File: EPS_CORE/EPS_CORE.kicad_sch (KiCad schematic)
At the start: 29 parts, among them J6301 VBUS, J7101 VBUS, J7102 BATT_PACK, J7103 BATT_PACK, J7104 VBUS, J7105 Chan, J7106 Chan, SW7101 Deploy, U7101 LP38690SDX-3.3/NOPB

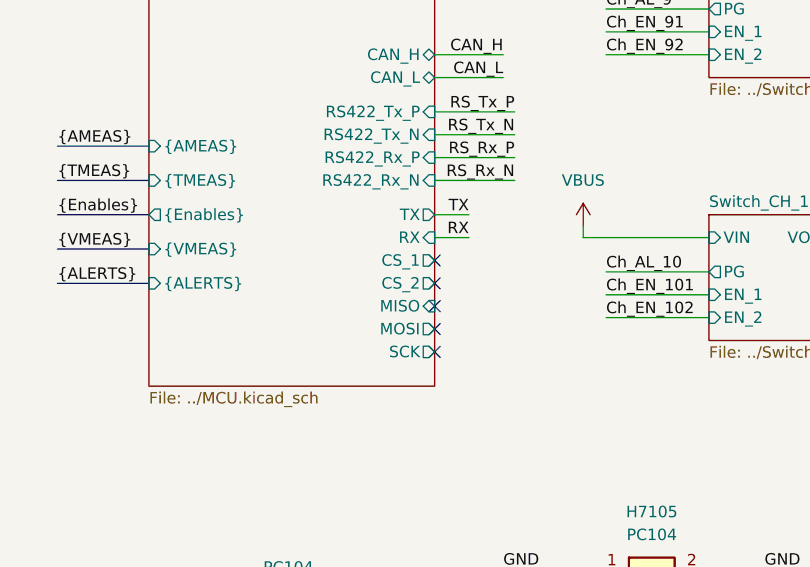
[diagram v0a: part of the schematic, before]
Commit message: added universal switch, added simples current source, reworked test schematic and pcb
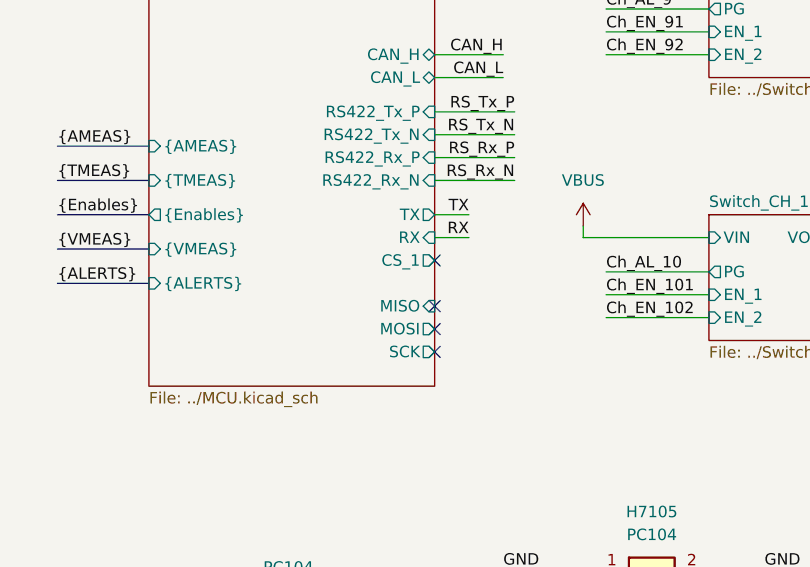
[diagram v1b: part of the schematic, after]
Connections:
- no-connect marks 23 -> 22
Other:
- sheet MCU ports: added none; removed CS_2
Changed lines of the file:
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@@
 	)
 	(no_connect
-		(at 184.15 60.96)
-	)
-	(no_connect
 		(at 250.19 118.11)
 	)
@@
 			(effects
 				(font
-					(size 1.27 1.27)
-				)
-				(justify right)
-			)
-		)
-		(pin "CS_2" output
-			(at 184.15 60.96 0)
-			(effects
-				(font

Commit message: progress on CORE pcb
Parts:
- removed J6301, J7104: VBUS, Connector_Harwin:Harwin_Gecko-G125-FVX1205L0X_2x06_P1.25mm_Vertical, symbol Connector_Generic:Conn_02x06_Top_Bottom
- removed J7105, J7106: Chan, Connector_Molex:Molex_CLIK-Mate_502494-0470_1x04-1MP_P2.00mm_Horizontal, symbol Connector_Generic:Conn_01x04
- added J106: OUT, Connector_Harwin:Harwin_Gecko-G125-MVX1005L1X_2x05_P1.25mm_Vertical, symbol Connector_Generic:Conn_02x05_Top_Bottom
- J105: renamed from J7101; now not fitted; now left out of the parts list
- renumbered C7106 to C101, C7101 to C102, C7105 to C103, C7103 to C104, C7102 to C105, C7104 to C106, FID7101 to FID101, FID7102 to FID102, H7105 to H101, H7106 to H102, H7101 to H103, H7102 to H104, H7103 to H105, H7104 to H106, J7102 to J102, J7103 to J104, PCB7101 to PCB101, R7104 to R101, R7105 to R102, R7101 to R103, R7102 to R104, R7103 to R105, SW7101 to SW101, U7101 to U101
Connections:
- net AMEAS_2: now also H101.5 (Pin_5); no longer H101.7 (Pin_7)
- net AMEAS_3: now also H101.7 (Pin_7); no longer H101.11 (Pin_11)
- net AMEAS_4: now also H101.9 (Pin_9); no longer H101.5 (Pin_5)
- net AMEAS_5: now also H101.11 (Pin_11); no longer H101.9 (Pin_9)
- net BUS: now also H102.41 (Pin_41), H102.42 (Pin_42), H102.43 (Pin_43), H102.44 (Pin_44), H102.45 (Pin_45), H102.46 (Pin_46)
- net Ch_EN_31: now also H102.29 (Pin_29); no longer H101.39 (Pin_39)
- net Ch_EN_32: now also H102.33 (Pin_33); no longer H101.43 (Pin_43)
- net Ch_EN_61: now also H102.31 (Pin_31); no longer H101.41 (Pin_41)
- net Ch_EN_62: now also H102.35 (Pin_35); no longer H101.45 (Pin_45)
- net Ch_EN_7x: now also H102.37 (Pin_37); no longer H101.47 (Pin_47)
- net Ch_EN_8x: now also H102.38 (Pin_38); no longer H101.49 (Pin_49)
- net Ch_V_1: now also H102.13 (Pin_13); no longer H101.22 (Pin_22)
- net Ch_V_2: now also H102.11 (Pin_11); no longer H101.26 (Pin_26)
- net Ch_V_3: now also H102.9 (Pin_9); no longer H101.30 (Pin_30)
- net Ch_V_4: now also H102.7 (Pin_7); no longer H101.24 (Pin_24)
- net Ch_V_5: now also H102.5 (Pin_5); no longer H101.28 (Pin_28)
- net Ch_V_6: now also H102.3 (Pin_3); no longer H101.32 (Pin_32)
- net Ch_V_7: now also H101.24 (Pin_24); no longer H101.34 (Pin_34)
- net Ch_V_8: now also H101.22 (Pin_22); no longer H101.36 (Pin_36)
- net Channel_10: now also J106.4 (Pin_4), J106.5 (Pin_5)
- net Channel_9: now also J106.1 (Pin_1), J106.2 (Pin_2)
- net GND: now also H101.39 (Pin_39), H101.41 (Pin_41), H101.43 (Pin_43), H101.44 (Pin_44), H101.45 (Pin_45), H101.46 (Pin_46), H101.47 (Pin_47), H101.48 (Pin_48), H101.49 (Pin_49), H101.50 (Pin_50), H102.17 (Pin_17), H102.19 (Pin_19), H102.21 (Pin_21), H102.23 (Pin_23), H102.25 (Pin_25), H102.36 (Pin_36), H102.39 (Pin_39), H102.40 (Pin_40), J106.10 (Pin_10), J106.3 (Pin_3), J106.6 (Pin_6), J106.7 (Pin_7), J106.8 (Pin_8), J106.9 (Pin_9); no longer H102.29 (Pin_29), H102.44 (Pin_44), H102.46 (Pin_46), H102.48 (Pin_48), H102.50 (Pin_50), H102.52 (Pin_52)
- net MPPT_~{EN}: now also H102.27 (Pin_27); no longer H102.17 (Pin_17)
- net SOL_EN_1: now also H101.36 (Pin_36); no longer H102.3 (Pin_3)
- net SOL_EN_2: now also H101.34 (Pin_34); no longer H102.5 (Pin_5)
- net SOL_EN_3: now also H101.32 (Pin_32); no longer H102.7 (Pin_7)
- net SOL_EN_4: now also H101.30 (Pin_30); no longer H102.9 (Pin_9)
- net SOL_EN_5: now also H101.28 (Pin_28); no longer H102.11 (Pin_11)
- net SOL_EN_6: now also H101.26 (Pin_26); no longer H102.13 (Pin_13)
- net VBUS: now also H102.48 (Pin_48), H102.50 (Pin_50), H102.52 (Pin_52); no longer H101.44 (Pin_44), H101.46 (Pin_46), H101.48 (Pin_48), H101.50 (Pin_50), H102.43 (Pin_43), H102.45 (Pin_45)
- no-connect marks 22 -> 7
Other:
- moved on the sheet: H101, H102

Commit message: nearly finnished CORE pcb
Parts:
- added FID103, FID104: Fiducial, Fiducial:Fiducial_1mm_Mask2mm, symbol Mechanical:Fiducial
- added J101: CAN, Connector_Molex:Molex_PicoBlade_53261-0471_1x04-1MP_P1.25mm_Horizontal, symbol Connector_Generic_MountingPin:Conn_01x04_MountingPin
- added J103: RS-485, Connector_Molex:Molex_PicoBlade_53261-0471_1x04-1MP_P1.25mm_Horizontal, symbol Connector_Generic_MountingPin:Conn_01x04_MountingPin
- J102, J104: footprint Connector_Harwin:Harwin_Gecko-G125-FVX1605L0X_2x08_P1.25mm_Vertical -> Outlines:G125-MH11605L1P
- J106: footprint Connector_Harwin:Harwin_Gecko-G125-MVX1005L1X_2x05_P1.25mm_Vertical -> Outlines:G125-MH11605L1P
- R101, R102: footprint Resistor_SMD:R_0603_1608Metric_Pad0.98x0.95mm_HandSolder -> Resistor_SMD:R_1210_3225Metric_Pad1.30x2.65mm_HandSolder
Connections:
- net +3V3: no longer J102.8 (Pin_8), J104.8 (Pin_8)
- net AMEAS_2: now also H102.4 (Pin_4); no longer H101.5 (Pin_5)
- net AMEAS_3: now also H101.5 (Pin_5); no longer H101.7 (Pin_7)
- net AMEAS_4: now also H102.6 (Pin_6); no longer H101.9 (Pin_9)
- net AMEAS_5: now also H101.7 (Pin_7); no longer H101.11 (Pin_11)
- net AMEAS_6: now also H102.8 (Pin_8); no longer H101.13 (Pin_13)
- net AMEAS_7: now also H101.9 (Pin_9); no longer H101.15 (Pin_15)
- net AMEAS_8: now also H102.10 (Pin_10); no longer H101.17 (Pin_17)
- net AMEAS_SOL_1: now also H101.17 (Pin_17); no longer H102.18 (Pin_18)
- net AMEAS_SOL_2: now also H101.15 (Pin_15); no longer H102.20 (Pin_20)
- net AMEAS_SOL_3: now also H102.14 (Pin_14); no longer H102.22 (Pin_22)
- net AMEAS_SOL_4: now also H101.13 (Pin_13); no longer H102.24 (Pin_24)
- net AMEAS_SOL_5: now also H102.12 (Pin_12); no longer H102.26 (Pin_26)
- net AMEAS_SOL_6: now also H101.11 (Pin_11); no longer H102.28 (Pin_28)
- net BATT_ALERT_1: now also J102.5 (Pin_5)
- net BATT_ALERT_2: now also J104.5 (Pin_5)
- net CAN_H: now also J101.3 (Pin_3)
- net CAN_L: now also J101.2 (Pin_2)
- net Ch_AL_1: now also H102.3 (Pin_3); no longer H101.4 (Pin_4)
- net Ch_AL_2: now also H102.5 (Pin_5); no longer H101.8 (Pin_8)
- net Ch_AL_3: now also H102.7 (Pin_7); no longer H101.12 (Pin_12)
- net Ch_AL_4: now also H102.9 (Pin_9); no longer H101.6 (Pin_6)
- net Ch_AL_5: now also H101.18 (Pin_18); no longer H101.10 (Pin_10)
- net Ch_AL_6: now also H101.16 (Pin_16); no longer H101.14 (Pin_14)
- net Ch_AL_7: now also H102.11 (Pin_11); no longer H101.16 (Pin_16)
- net Ch_AL_8: now also H102.13 (Pin_13); no longer H101.18 (Pin_18)
- net Ch_EN_11: now also H101.29 (Pin_29); no longer H101.21 (Pin_21)
- net Ch_EN_12: now also H101.27 (Pin_27); no longer H101.25 (Pin_25)
- net Ch_EN_21: now also H101.30 (Pin_30); no longer H101.29 (Pin_29)
- net Ch_EN_22: now also H101.23 (Pin_23); no longer H101.33 (Pin_33)
- net Ch_EN_32: now also H101.25 (Pin_25); no longer H102.33 (Pin_33)
- net Ch_EN_41: now also H101.31 (Pin_31); no longer H101.23 (Pin_23)
- net Ch_EN_42: now also H102.27 (Pin_27); no longer H101.27 (Pin_27)
- net Ch_EN_51: now also H102.34 (Pin_34); no longer H101.31 (Pin_31)
- net Ch_EN_52: now also H102.32 (Pin_32); no longer H101.35 (Pin_35)
- net Ch_EN_61: now also H102.33 (Pin_33); no longer H102.31 (Pin_31)
- net Ch_EN_62: now also H102.31 (Pin_31); no longer H102.35 (Pin_35)
- net Ch_EN_7x: now also H101.26 (Pin_26); no longer H102.37 (Pin_37)
- net Ch_EN_8x: now also H101.28 (Pin_28); no longer H102.38 (Pin_38)
- net Ch_V_1: now also H101.14 (Pin_14); no longer H102.13 (Pin_13)
- net Ch_V_2: now also H101.12 (Pin_12); no longer H102.11 (Pin_11)
- net Ch_V_3: now also H101.10 (Pin_10); no longer H102.9 (Pin_9)
- net Ch_V_4: now also H101.8 (Pin_8); no longer H102.7 (Pin_7)
- net Ch_V_5: now also H101.6 (Pin_6); no longer H102.5 (Pin_5)
- net Ch_V_6: now also H101.4 (Pin_4); no longer H102.3 (Pin_3)
- net Ch_V_7: now also H102.19 (Pin_19); no longer H101.24 (Pin_24)
- net Ch_V_8: now also H102.21 (Pin_21); no longer H101.22 (Pin_22)
- net GND: now also H101.22 (Pin_22), H101.24 (Pin_24), J102.13 (Pin_13), J102.15 (Pin_15), J104.13 (Pin_13), J104.15 (Pin_15); no longer H102.19 (Pin_19), H102.21 (Pin_21), J102.4 (Pin_4), J102.6 (Pin_6), J104.4 (Pin_4), J104.6 (Pin_6)
- net HEAT_BATT_1: now also J102.8 (Pin_8); no longer J102.16 (Pin_16)
- net HEAT_BATT_2: now also J104.8 (Pin_8); no longer J104.16 (Pin_16)
- net MPPT_~{EN}: now also H101.21 (Pin_21); no longer H102.27 (Pin_27)
- net RS_Rx_N: now also J103.4 (Pin_4)
- net RS_Rx_P: now also J103.3 (Pin_3)
- net RS_Tx_N: now also J103.2 (Pin_2)
- net RS_Tx_P: now also J103.1 (Pin_1)
- net SCL: now also J102.6 (Pin_6), J104.6 (Pin_6); no longer J102.15 (Pin_15), J104.15 (Pin_15)
- net SHIELD: now also J101.MP (MountPin), J103.MP (MountPin)
- net SOL_EN_1: now also H101.33 (Pin_33); no longer H101.36 (Pin_36)
- net SOL_EN_3: now also H101.35 (Pin_35); no longer H101.32 (Pin_32)
- net SOL_EN_4: now also H101.36 (Pin_36); no longer H101.30 (Pin_30)
- net SOL_EN_5: now also H102.35 (Pin_35); no longer H101.28 (Pin_28)
- net SOL_EN_6: now also H102.38 (Pin_38); no longer H101.26 (Pin_26)
- net SOL_STAT_1: now also H102.37 (Pin_37); no longer H102.34 (Pin_34)
- net SOL_STAT_2: now also H101.32 (Pin_32); no longer H102.32 (Pin_32)
- net TMEAS_BATT_1: now also J102.4 (Pin_4); no longer J102.13 (Pin_13)
- net TMEAS_BATT_2: now also J104.4 (Pin_4); no longer J104.13 (Pin_13)
- net VMEAS_SOL_1: now also H102.18 (Pin_18); no longer H102.4 (Pin_4)
- net VMEAS_SOL_2: now also H102.20 (Pin_20); no longer H102.6 (Pin_6)
- net VMEAS_SOL_3: now also H102.22 (Pin_22); no longer H102.8 (Pin_8)
- net VMEAS_SOL_4: now also H102.24 (Pin_24); no longer H102.10 (Pin_10)
- net VMEAS_SOL_5: now also H102.26 (Pin_26); no longer H102.12 (Pin_12)
- net VMEAS_SOL_6: now also H102.28 (Pin_28); no longer H102.14 (Pin_14)
- removed net ALERT: J102.5 (Pin_5), J104.5 (Pin_5)
- new net BATT_BOOT: J102.16 (Pin_16), J104.16 (Pin_16)
- no-connect marks 7 -> 9

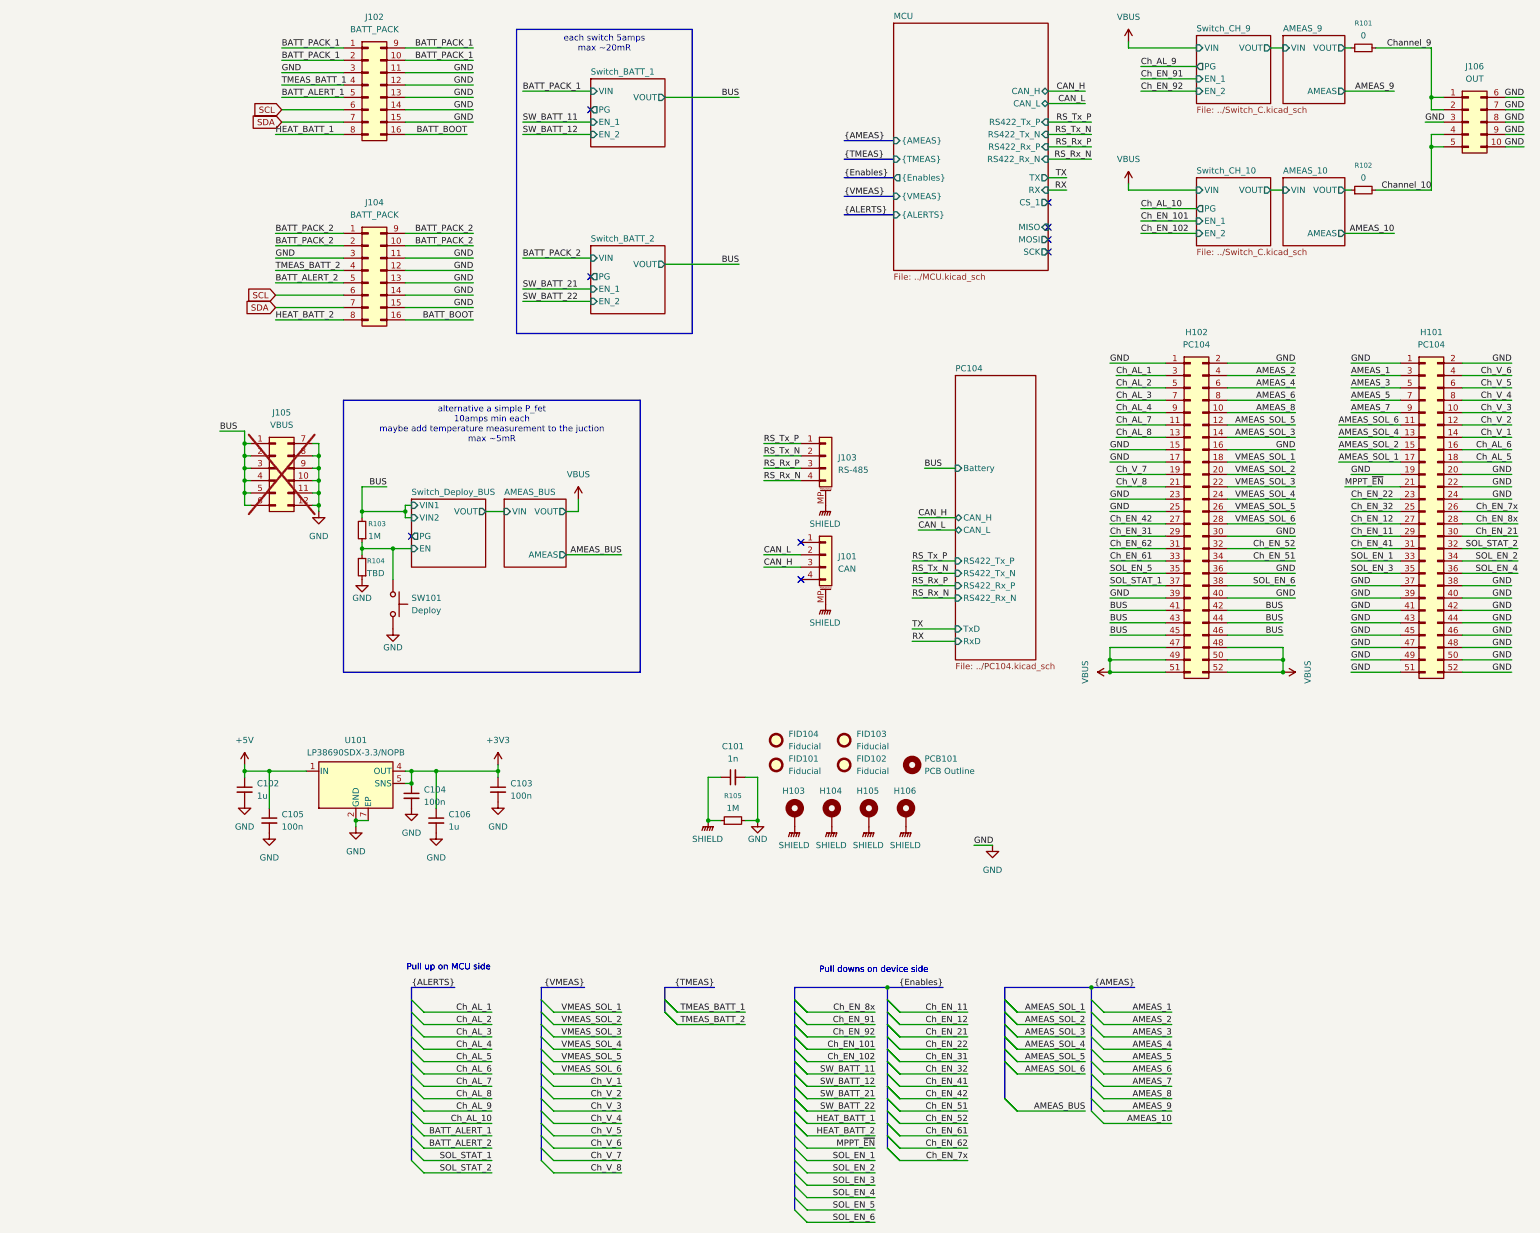
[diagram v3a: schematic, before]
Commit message: pcb progres for all components
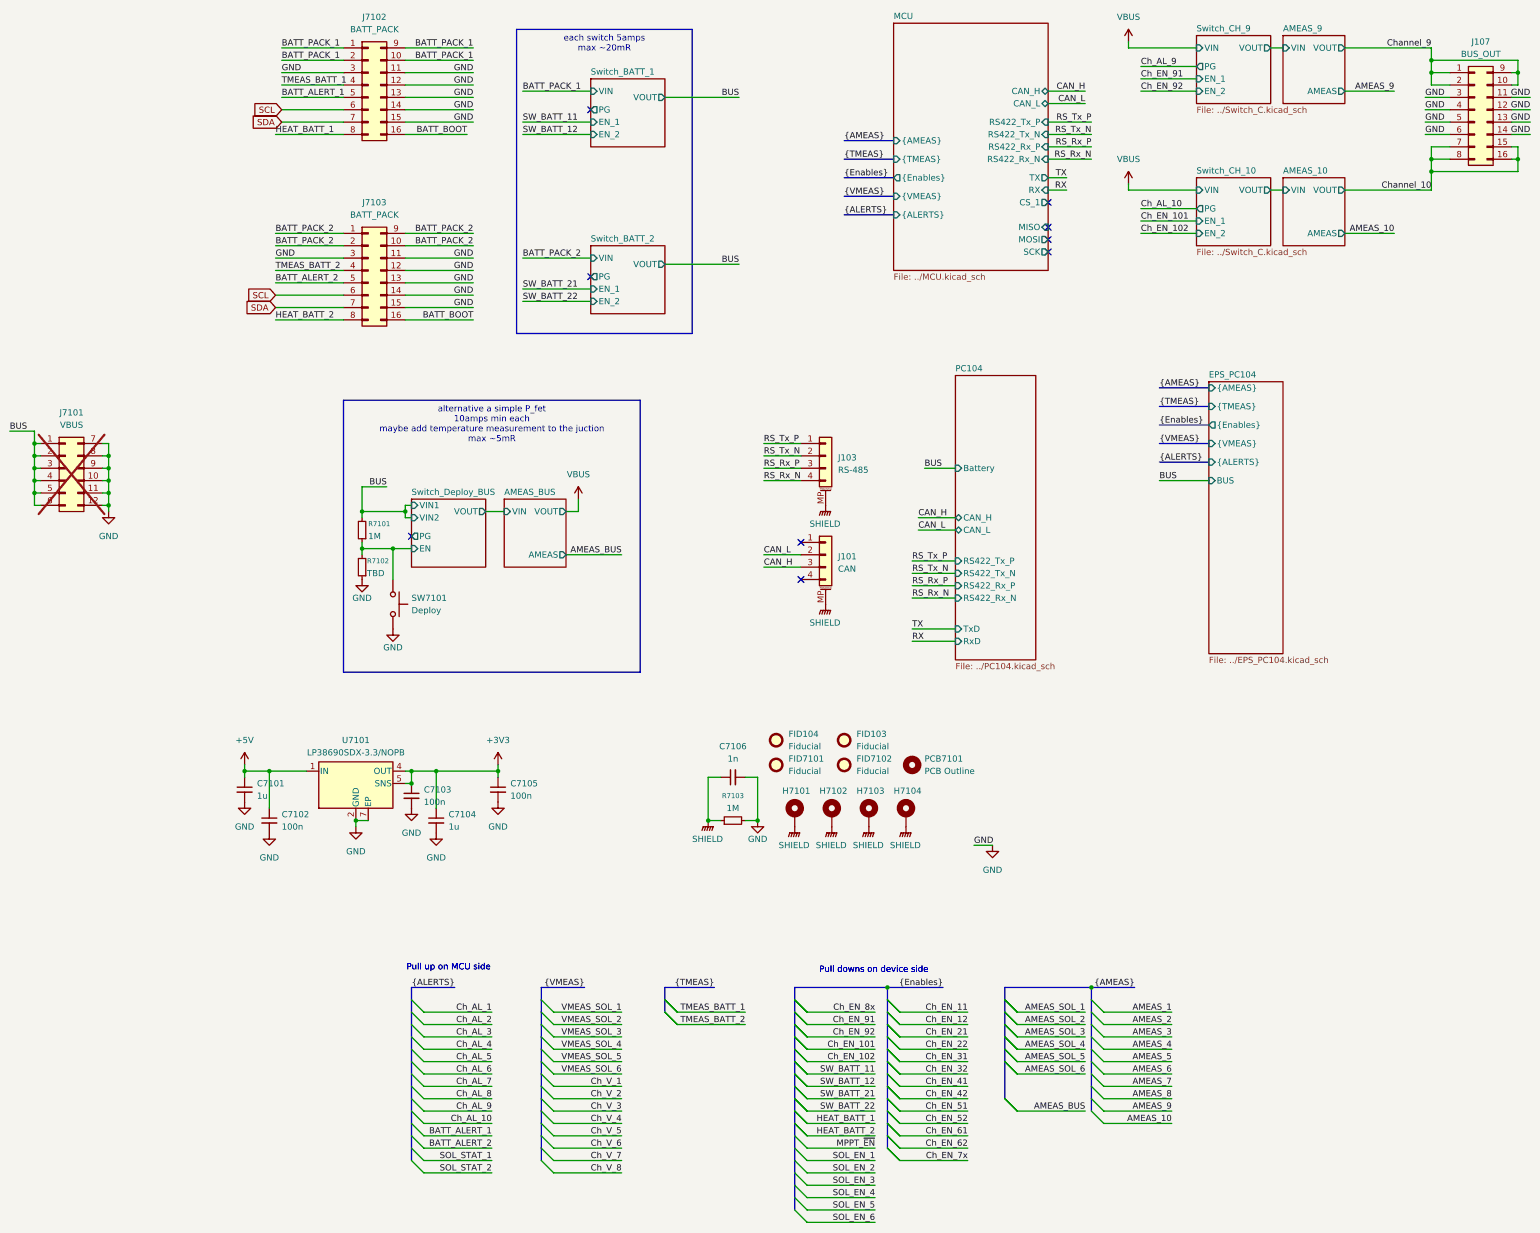
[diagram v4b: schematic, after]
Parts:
- removed H101, H102: PC104, Connector_PinSocket_2.54mm:PinSocket_2x26_P2.54mm_Vertical, symbol Connector_Generic:Conn_02x26_Odd_Even
- removed J106: OUT, Outlines:G125-MH11605L1P, symbol Connector_Generic:Conn_02x05_Top_Bottom
- removed R101, R102: 0, Resistor_SMD:R_1210_3225Metric_Pad1.30x2.65mm_HandSolder, symbol Device:R_Small
- added J107: BUS_OUT, Outlines:G125-MH11605L1P, symbol Connector_Generic:Conn_02x08_Top_Bottom
- renumbered C102 to C7101, C105 to C7102, C104 to C7103, C106 to C7104, C103 to C7105, C101 to C7106, FID101 to FID7101, FID102 to FID7102, H103 to H7101, H104 to H7102, H105 to H7103, H106 to H7104, J105 to J7101, J102 to J7102, J104 to J7103, PCB101 to PCB7101, R103 to R7101, R104 to R7102, R105 to R7103, SW101 to SW7101, U101 to U7101
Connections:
- net Channel_10: now also J107.15 (Pin_15), J107.16 (Pin_16), J107.7 (Pin_7), J107.8 (Pin_8)
- net Channel_9: now also J107.1 (Pin_1), J107.10 (Pin_10), J107.2 (Pin_2), J107.9 (Pin_9)
- net GND: now also J107.11 (Pin_11), J107.12 (Pin_12), J107.13 (Pin_13), J107.14 (Pin_14), J107.3 (Pin_3), J107.4 (Pin_4), J107.5 (Pin_5), J107.6 (Pin_6)
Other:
- added sheet EPS_PC104 (../EPS_PC104.kicad_sch)
- moved on the sheet: J7101
